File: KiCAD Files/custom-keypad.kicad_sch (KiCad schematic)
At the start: 10 parts, among them IC2 USBLC6-2SC6, J1 UJ32-C-H-G-H2-SMT-TR, SW1 SW_Push, SW2 SW_Push, SW3 SW_Push, SW4 SW_Push, SW8 SW_Push, SW9 SW_Push

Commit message: initial schematic and pcb designs
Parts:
- added C8: 2.2n, Capacitor_SMD:C_0805_2012Metric_Pad1.18x1.45mm_HandSolder, symbol CustomSymbols:C
- added J2: EN11-HSM1BF20, EN11HSM1BF20, symbol CustomSymbols:EN11-HSM1BF20
- added R5: 1M, Resistor_SMD:R_0805_2012Metric_Pad1.20x1.40mm_HandSolder, symbol CustomSymbols:R_US
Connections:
- net +3.3V: now also J2.D1
- net GND: now also C8.2, J2.C1, R5.2
- net PA1/Caps Lock renamed PA1/Key 4
- net PA1/Dash renamed PA1/Key 6
- net PA1/Dot renamed PA1/Key 5
- net PA1/Enter renamed PA1/Key 2
- net PA1/Esc renamed PA1/Key 1
- net PA1/Space renamed PA1/Key 3
- new net: C8.1, J2.MH2, R5.1
- new net PA1/Rotary A: J2.A1
- new net PA1/Rotary B: J2.B1
- new net PA1/Rotary SW: J2.E1
- no-connect marks 15 -> 16
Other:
- note added: "Rotary Encoder"
- moved on the sheet: SW4

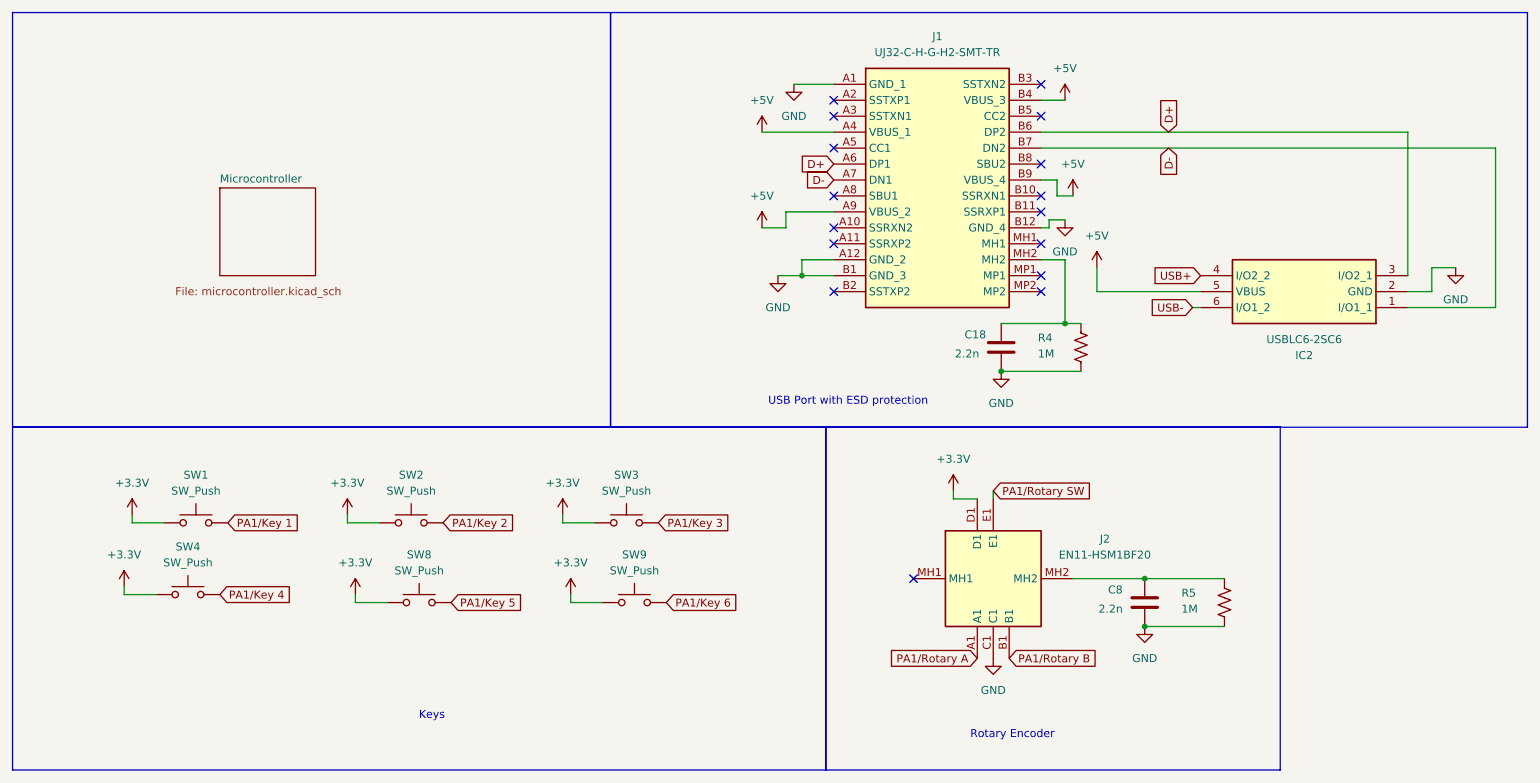
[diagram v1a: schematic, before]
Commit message: finished pcb and diagram, need to double check before producing
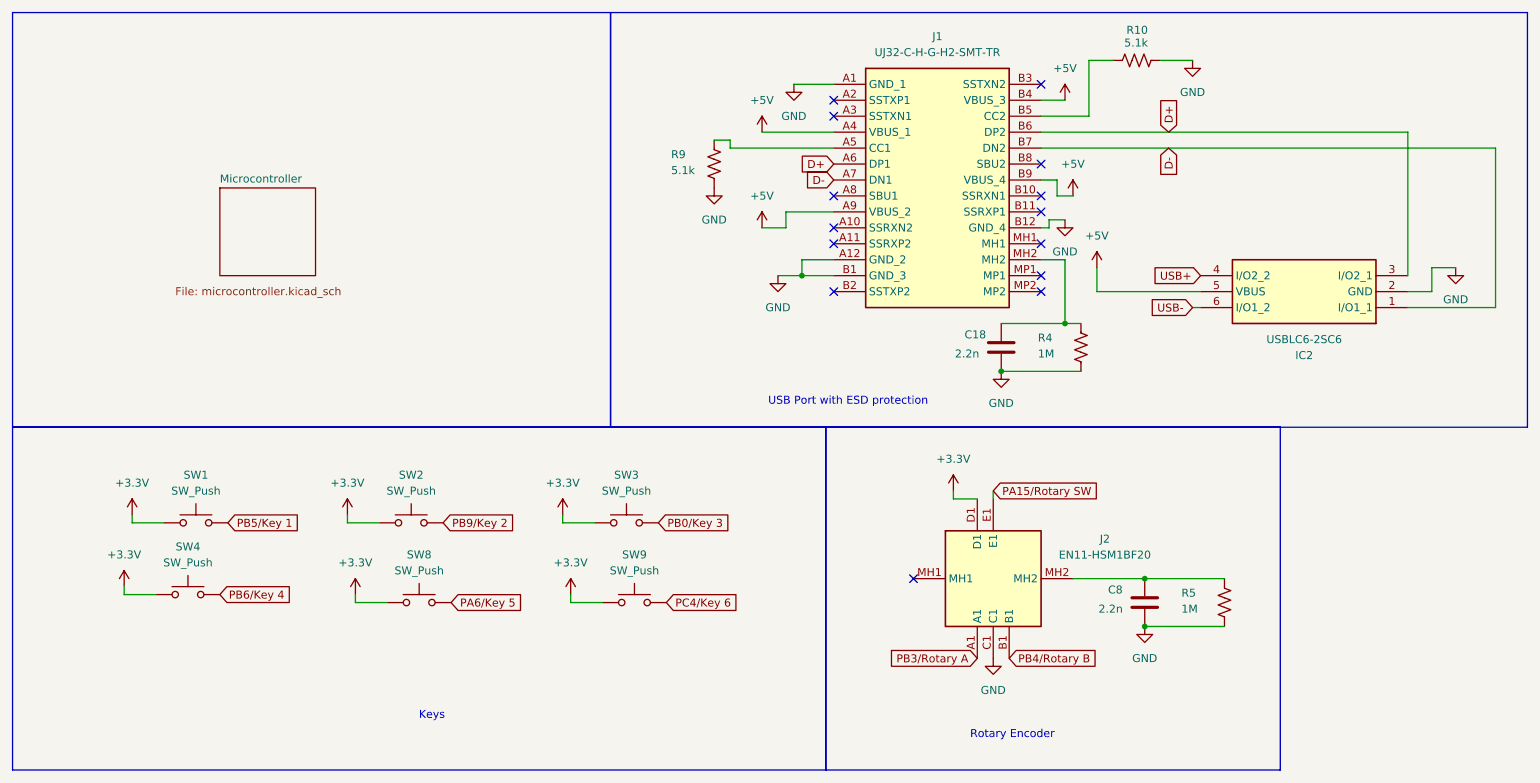
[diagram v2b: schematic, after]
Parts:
- added R10, R9: 5.1k, Resistor_SMD:R_0805_2012Metric_Pad1.20x1.40mm_HandSolder, symbol CustomSymbols:R_US
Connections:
- net GND: now also R10.2, R9.2
- net at J1.A5 (CC1): now also R9.1
- net at J1.B5 (CC2): now also R10.1
- net PA1/Key 1 renamed PB5/Key 1
- net PA1/Key 2 renamed PB9/Key 2
- net PA1/Key 3 renamed PB0/Key 3
- net PA1/Key 4 renamed PB6/Key 4
- net PA1/Key 5 renamed PA6/Key 5
- net PA1/Key 6 renamed PC4/Key 6
- net PA1/Rotary A renamed PB3/Rotary A
- net PA1/Rotary B renamed PB4/Rotary B
- net PA1/Rotary SW renamed PA15/Rotary SW
- no-connect marks 16 -> 14
